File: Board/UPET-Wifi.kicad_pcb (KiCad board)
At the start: 2 copper layers, 45.8 x 25.4 mm, 21 parts, among them J1 Conn_01x06, J3 Conn_01x09, Q1 S8050, Q2 S8050, U1 ESP32-C3-WROOM-02, U2 SC16IS752IPW, U3 1.8432 MHz

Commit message: production files
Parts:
- added JP3: SolderJumper_2_Open, Jumper:SolderJumper-2_P1.3mm_Open_RoundedPad1.0x1.5mm, F.Cu at (137.8, 85.5)
- moved R2 0.51 mm to (134.0, 85.5)
- moved R3 0.51 mm to (128.0, 85.3)
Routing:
- net /RXD: track 13.8 -> 22.3 mm
- net Net-(J1-Pin_3): track 8.44 -> 9.82 mm
- added copper zone on F.Cu, net GND
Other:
- board text added: "3.3V"

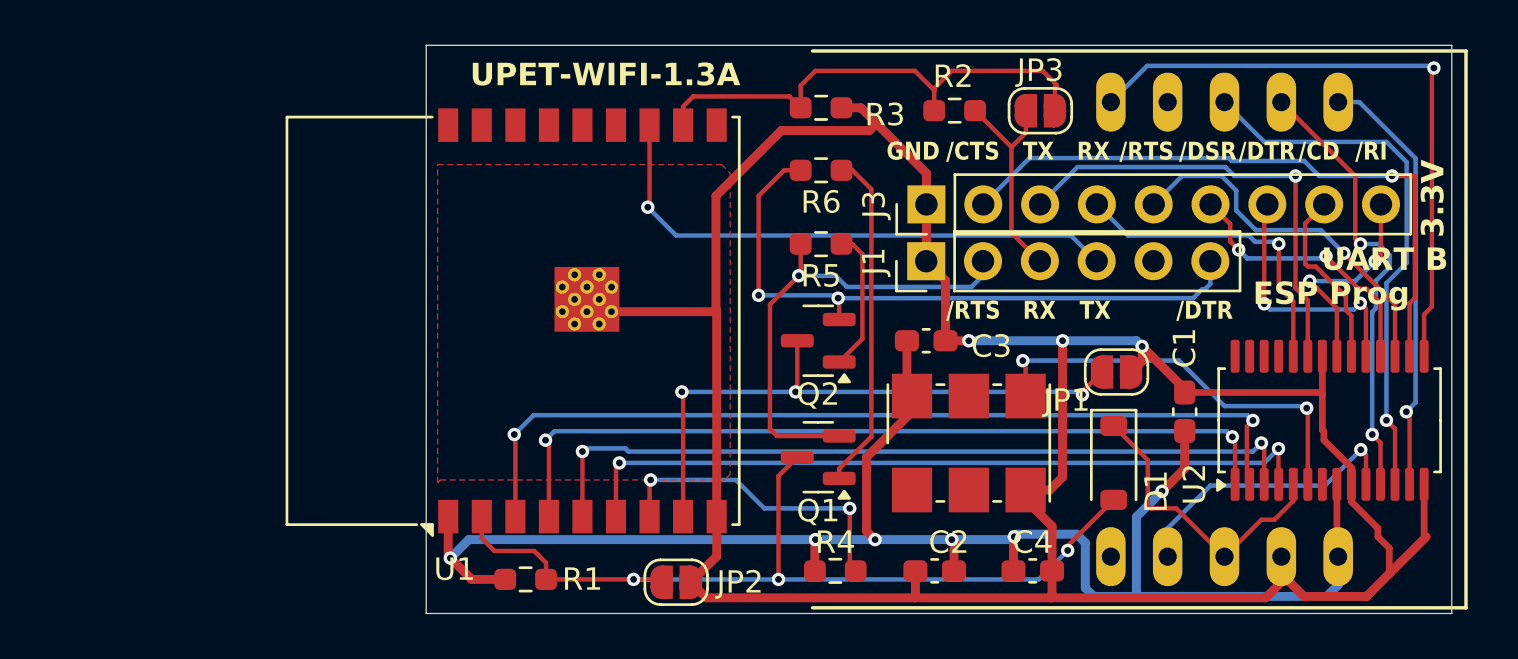
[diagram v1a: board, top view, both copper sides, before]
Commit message: replace ESP32-WROOM with an ESP32-VROVER-E
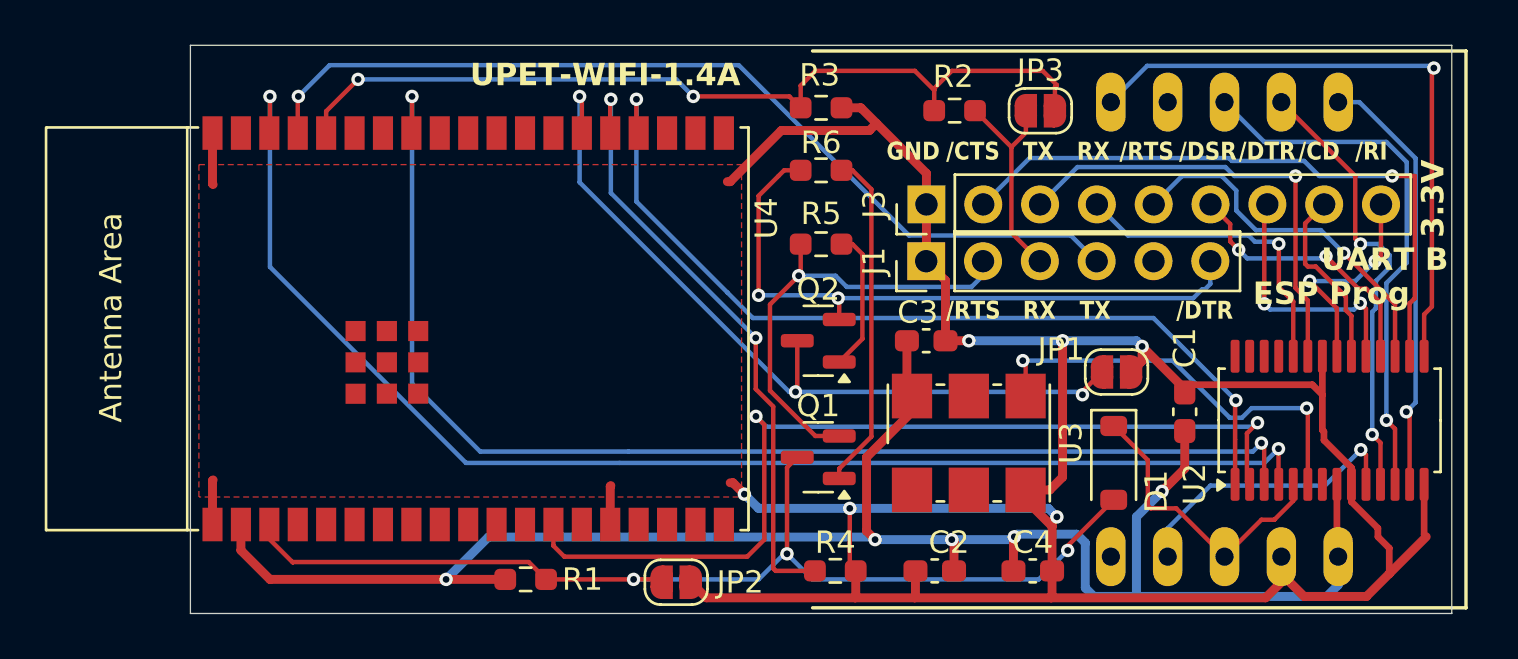
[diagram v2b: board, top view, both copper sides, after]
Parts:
- removed U1: ESP32-C3-WROOM-02, RF_Module:ESP32-C3-WROOM-02
- added U4: ESP32-WROVER-E, PCM_Espressif:ESP32-WROVER-E, F.Cu at (109.1, 95.2)
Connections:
- net Net-(J1-Pin_2) renamed //PRTS
- net Net-(J1-Pin_3) renamed /PRX
- R4 pad 1: VCC -> Net-(U4-ADC2_CH2/GPIO2)
- R4 pad 2: Net-(U1-IO8) -> GND
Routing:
- net Net-(U4-ADC2_CH2/GPIO2): track 0.00 -> 27.4 mm, vias 0 -> 2
- net /RXA: track 33.8 -> 59.8 mm
- net /TXA: track 35.4 -> 55.8 mm
- net /RXD: track 22.3 -> 39.1 mm, vias 0 -> 2
- net /TXD: track 24.8 -> 41.5 mm
- net Net-(U1-IO8): track 14.0 -> 0.00 mm, vias 2 -> 0
- net Net-(D1-A): track 39.1 -> 47.5 mm
- net Net-(JP1-B): track 27.3 -> 35.6 mm
- net VCC: track 74.7 -> 82.8 mm, vias 6 -> 5
- net //RTSA: track 36.6 -> 40.4 mm
- net //CTSA: track 40.2 -> 42.2 mm
- net GND: track 130.6 -> 132.4 mm, vias 3 -> 6
- net //PRTS: track 21.4 -> 20.3 mm
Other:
- board size 45.8 x 25.4 mm -> 56.4 x 25.4 mm
- board text added: "U3"
- board text added: "UPET-WIFI-1.4A"
- board text removed: "UPET-WIFI-1.3A"
